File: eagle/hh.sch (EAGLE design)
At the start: 6 parts

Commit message: testing final design
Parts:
- renumbered U$1 to ESP12E_DEVKIT
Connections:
- net N$8: now also ESP12E_DEVKIT.D0; no longer ESP12E_DEVKIT.D5
- net N$9: now also ESP12E_DEVKIT.RX; no longer ESP12E_DEVKIT.D6
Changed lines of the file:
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@@
 <part name="S3" library="switch-omron" deviceset="10-XX" device=""/>
 <part name="S4" library="switch-omron" deviceset="10-XX" device=""/>
-<part name="U$1" library="ESP12E_DEVKIT" deviceset="ESP12E_DEVKIT" device=""/>
+<part name="ESP12E_DEVKIT" library="ESP12E_DEVKIT" deviceset="ESP12E_DEVKIT" device=""/>
 <part name="FRAME1" library="frames" deviceset="FRAME_A_L" device=""/>
 <part name="GND2" library="supply1" deviceset="GND" device=""/>
@@
 <instance part="S3" gate="1" x="22.86" y="91.44"/>
 <instance part="S4" gate="1" x="22.86" y="68.58"/>
-<instance part="U$1" gate="G$1" x="119.38" y="93.98" rot="R180"/>
+<instance part="ESP12E_DEVKIT" gate="G$1" x="119.38" y="93.98" rot="R180"/>
 <instance part="FRAME1" gate="G$1" x="-22.86" y="-12.7"/>
 <instance part="FRAME1" gate="G$2" x="149.86" y="-12.7"/>
@@
 <net name="GND" class="0">
 <segment>
-<pinref part="U$1" gate="G$1" pin="GND@3"/>
+<pinref part="ESP12E_DEVKIT" gate="G$1" pin="GND@3"/>
 <pinref part="GND2" gate="1" pin="GND"/>
 <wire x1="101.6" y1="109.22" x2="78.74" y2="109.22" width="0.1524" layer="91"/>
@@
 <net name="N$1" class="0">
 <segment>
-<pinref part="U$1" gate="G$1" pin="3V3@2"/>
+<pinref part="ESP12E_DEVKIT" gate="G$1" pin="3V3@2"/>
 <wire x1="88.9" y1="129.54" x2="88.9" y2="124.46" width="0.1524" layer="91"/>
 <wire x1="88.9" y1="124.46" x2="101.6" y2="111.76" width="0.1524" layer="91"/>
@@
 <segment>
 <pinref part="JP1" gate="A" pin="1"/>
-<pinref part="U$1" gate="G$1" pin="3V3@1"/>
+<pinref part="ESP12E_DEVKIT" gate="G$1" pin="3V3@1"/>
 <wire x1="76.2" y1="43.18" x2="76.2" y2="63.5" width="0.1524" layer="91"/>
 <wire x1="76.2" y1="63.5" x2="101.6" y2="88.9" width="0.1524" layer="91"/>
@@
 <segment>
 <pinref part="JP1" gate="A" pin="2"/>
-<pinref part="U$1" gate="G$1" pin="GND@2"/>
+<pinref part="ESP12E_DEVKIT" gate="G$1" pin="GND@2"/>
 <wire x1="78.74" y1="43.18" x2="78.74" y2="68.58" width="0.1524" layer="91"/>
 <wire x1="78.74" y1="68.58" x2="101.6" y2="91.44" width="0.1524" layer="91"/>
@@
 <segment>
 <pinref part="JP1" gate="A" pin="4"/>
-<pinref part="U$1" gate="G$1" pin="D2"/>
+<pinref part="ESP12E_DEVKIT" gate="G$1" pin="D2"/>
 <wire x1="83.82" y1="43.18" x2="83.82" y2="63.5" width="0.1524" layer="91"/>
 <wire x1="83.82" y1="63.5" x2="101.6" y2="81.28" width="0.1524" layer="91"/>
@@
 <segment>
 <pinref part="JP1" gate="A" pin="3"/>
-<pinref part="U$1" gate="G$1" pin="D1"/>
+<pinref part="ESP12E_DEVKIT" gate="G$1" pin="D1"/>
 <wire x1="81.28" y1="43.18" x2="81.28" y2="58.42" width="0.1524" layer="91"/>
 <wire x1="81.28" y1="58.42" x2="101.6" y2="78.74" width="0.1524" layer="91"/>
@@
 <net name="N$2" class="0">
 <segment>
-<pinref part="U$1" gate="G$1" pin="D3"/>
+<pinref part="ESP12E_DEVKIT" gate="G$1" pin="D3"/>
 <pinref part="S4" gate="1" pin="S1"/>
 <wire x1="101.6" y1="83.82" x2="35.56" y2="83.82" width="0.1524" layer="91"/>
@@
 <net name="N$7" class="0">
 <segment>
-<pinref part="U$1" gate="G$1" pin="D4"/>
+<pinref part="ESP12E_DEVKIT" gate="G$1" pin="D4"/>
 <pinref part="S3" gate="1" pin="S1"/>
 <wire x1="101.6" y1="86.36" x2="35.56" y2="86.36" width="0.1524" layer="91"/>
@@
 <net name="N$8" class="0">
 <segment>
-<pinref part="U$1" gate="G$1" pin="D5"/>
 <pinref part="S2" gate="1" pin="S1"/>
-<wire x1="101.6" y1="93.98" x2="55.88" y2="93.98" width="0.1524" layer="91"/>
-<wire x1="55.88" y1="93.98" x2="25.4" y2="124.46" width="0.1524" layer="91"/>
+<wire x1="48.26" y1="124.46" x2="25.4" y2="124.46" width="0.1524" layer="91"/>
 <pinref part="S2" gate="1" pin="S"/>
 <wire x1="22.86" y1="124.46" x2="25.4" y2="124.46" width="0.1524" layer="91"/>
 <junction x="25.4" y="124.46"/>
+<wire x1="48.26" y1="124.46" x2="48.26" y2="76.2" width="0.1524" layer="91"/>
+<pinref part="ESP12E_DEVKIT" gate="G$1" pin="D0"/>
+<wire x1="48.26" y1="76.2" x2="101.6" y2="76.2" width="0.1524" layer="91"/>
 </segment>
 </net>
 <net name="N$9" class="0">
 <segment>
-<pinref part="U$1" gate="G$1" pin="D6"/>
 <pinref part="S1" gate="1" pin="S1"/>
-<wire x1="101.6" y1="96.52" x2="76.2" y2="96.52" width="0.1524" layer="91"/>
-<wire x1="76.2" y1="96.52" x2="25.4" y2="147.32" width="0.1524" layer="91"/>
+<wire x1="63.5" y1="147.32" x2="25.4" y2="147.32" width="0.1524" layer="91"/>
 <pinref part="S1" gate="1" pin="S"/>
 <wire x1="22.86" y1="147.32" x2="25.4" y2="147.32" width="0.1524" layer="91"/>
 <junction x="25.4" y="147.32"/>
+<pinref part="ESP12E_DEVKIT" gate="G$1" pin="RX"/>
+<wire x1="63.5" y1="147.32" x2="63.5" y2="104.14" width="0.1524" layer="91"/>
+<wire x1="63.5" y1="104.14" x2="101.6" y2="104.14" width="0.1524" layer="91"/>
 </segment>
 </net>

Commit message: tweaks
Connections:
- net N$8: now also ESP12E_DEVKIT.RX; no longer ESP12E_DEVKIT.D0
- net N$9: now also ESP12E_DEVKIT.TX; no longer ESP12E_DEVKIT.RX
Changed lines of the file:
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@@
 <wire x1="22.86" y1="124.46" x2="25.4" y2="124.46" width="0.1524" layer="91"/>
 <junction x="25.4" y="124.46"/>
-<wire x1="48.26" y1="124.46" x2="48.26" y2="76.2" width="0.1524" layer="91"/>
-<pinref part="ESP12E_DEVKIT" gate="G$1" pin="D0"/>
-<wire x1="48.26" y1="76.2" x2="101.6" y2="76.2" width="0.1524" layer="91"/>
+<wire x1="48.26" y1="124.46" x2="48.26" y2="104.14" width="0.1524" layer="91"/>
+<pinref part="ESP12E_DEVKIT" gate="G$1" pin="RX"/>
+<wire x1="48.26" y1="104.14" x2="101.6" y2="104.14" width="0.1524" layer="91"/>
 </segment>
 </net>
@@
 <wire x1="22.86" y1="147.32" x2="25.4" y2="147.32" width="0.1524" layer="91"/>
 <junction x="25.4" y="147.32"/>
-<pinref part="ESP12E_DEVKIT" gate="G$1" pin="RX"/>
-<wire x1="63.5" y1="147.32" x2="63.5" y2="104.14" width="0.1524" layer="91"/>
-<wire x1="63.5" y1="104.14" x2="101.6" y2="104.14" width="0.1524" layer="91"/>
+<wire x1="63.5" y1="147.32" x2="63.5" y2="106.68" width="0.1524" layer="91"/>
+<pinref part="ESP12E_DEVKIT" gate="G$1" pin="TX"/>
+<wire x1="63.5" y1="106.68" x2="101.6" y2="106.68" width="0.1524" layer="91"/>
 </segment>
 </net>

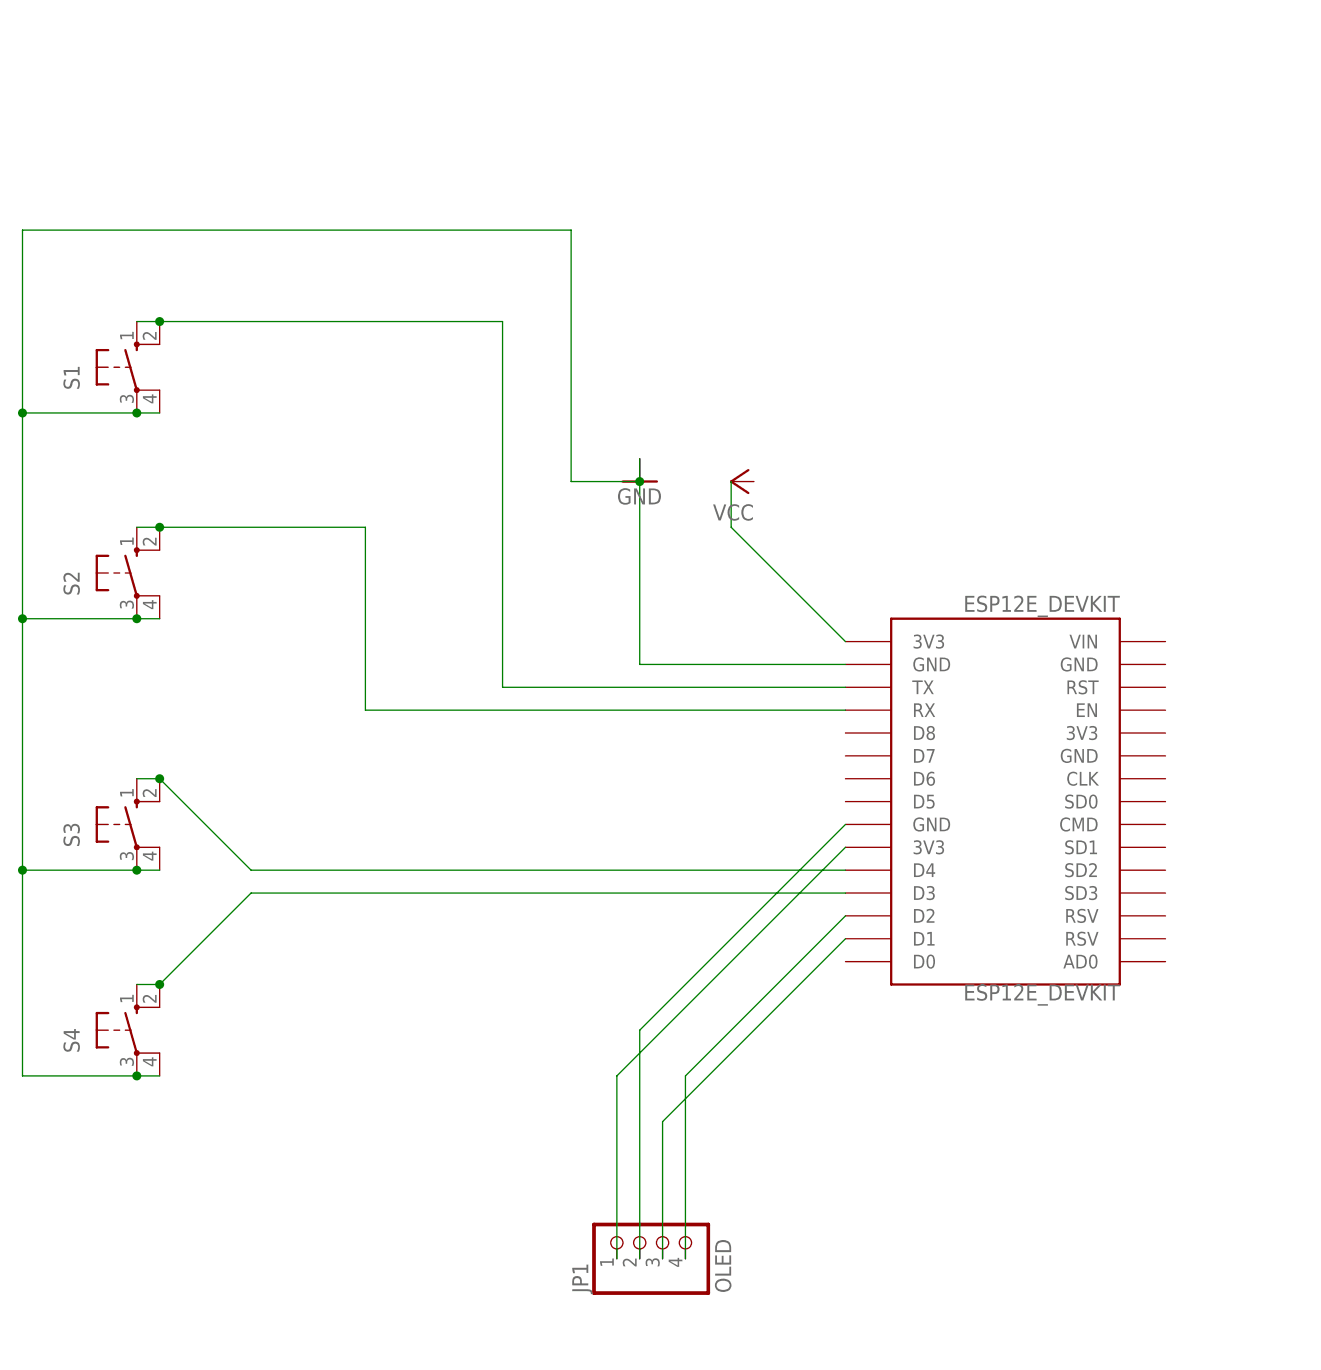
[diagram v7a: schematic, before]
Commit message: Added battery clips, fixed VIN, moved switches closer together to accommodate the battery clips, added a ground plane under the radio.
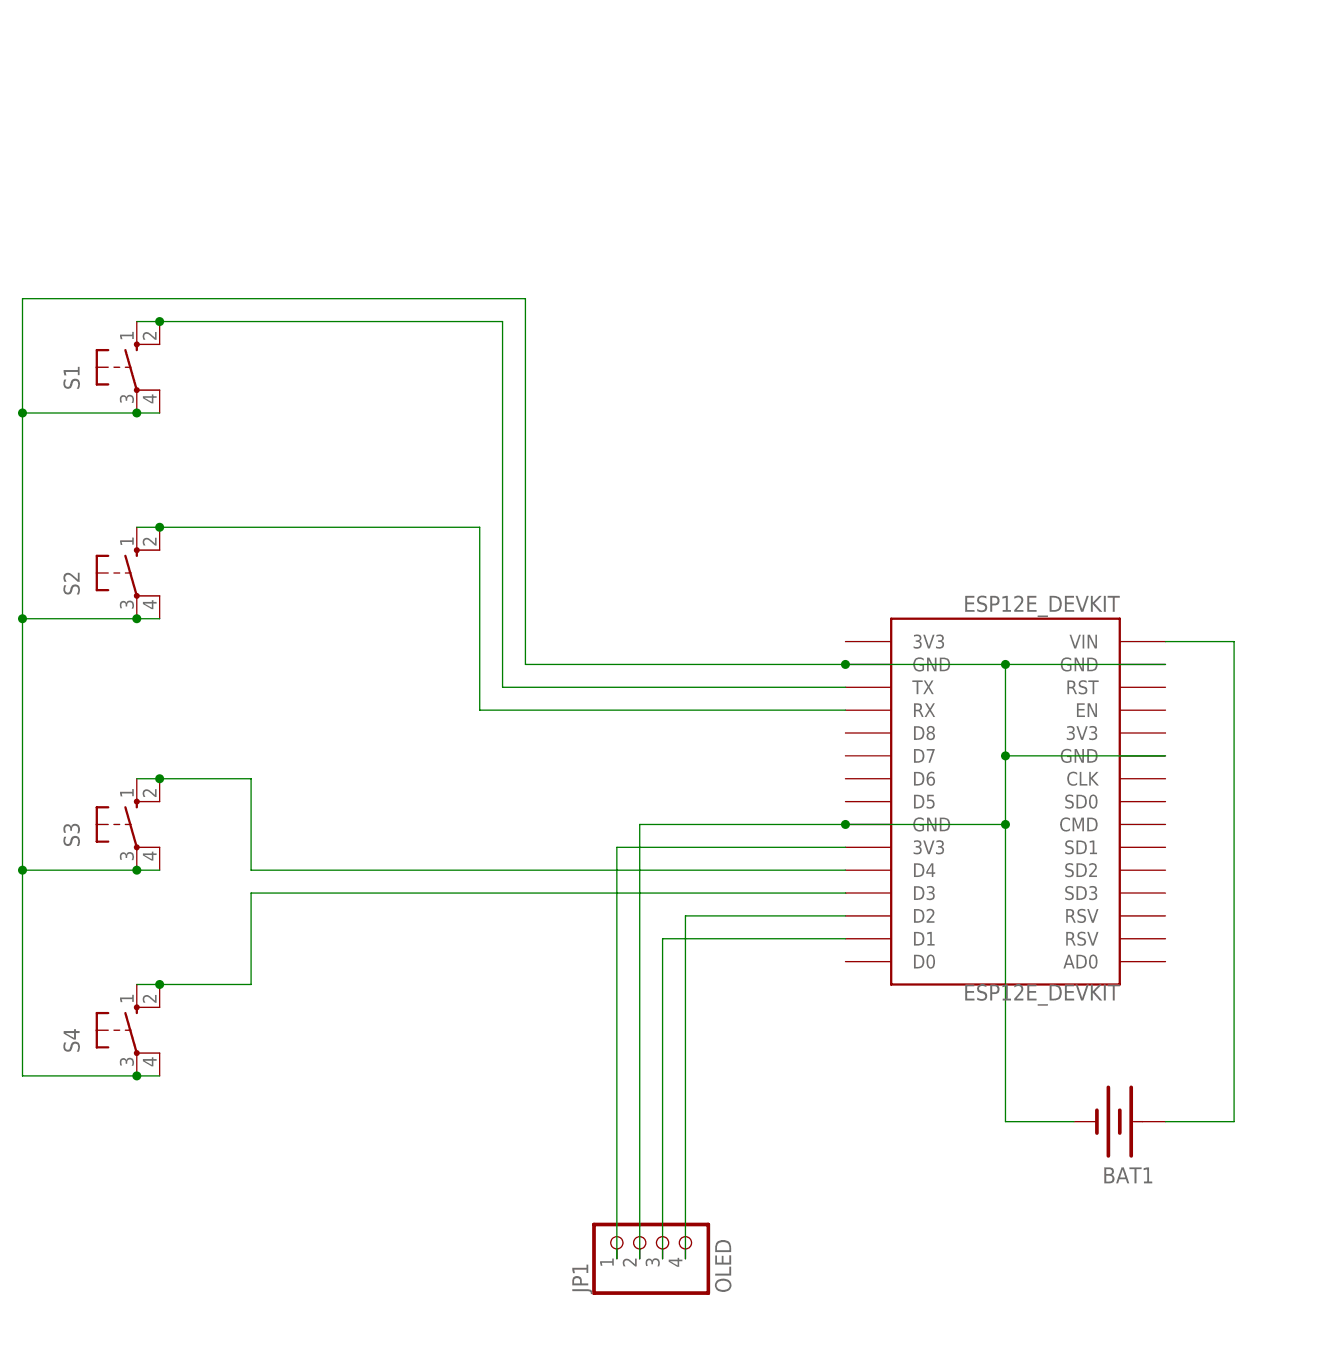
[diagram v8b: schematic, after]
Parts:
- added BAT1: (no value), SparkFun-Electromechanical:BATTERY18650
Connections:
- removed net GND: ESP12E_DEVKIT.GND@3, S1.P, S1.P1, S2.P, S2.P1, S3.P, S3.P1, S4.P, S4.P1
- net N$1: now also BAT1.-, ESP12E_DEVKIT.GND@0, ESP12E_DEVKIT.GND@1, ESP12E_DEVKIT.GND@2, ESP12E_DEVKIT.GND@3, JP1.2, S1.P, S1.P1, S2.P, S2.P1, S3.P, S3.P1, S4.P, S4.P1; no longer ESP12E_DEVKIT.3V3@2
- net N$4: now also BAT1.+, ESP12E_DEVKIT.VIN; no longer ESP12E_DEVKIT.GND@2, JP1.2
